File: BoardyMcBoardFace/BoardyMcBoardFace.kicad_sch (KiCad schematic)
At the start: 83 parts, among them J1 SMA, J2 ARM 10pin, J3 USB_B_Micro, SW1 SW_Push, U1 nRF24L01P, U2 STM32F103CBT6, U3 USBLC6-2SC6, U4 LM393, U5 AMS1117-5.0, U6 AMS1117-3.3, U7 USBLC6-2SC6, U8 USBLC6-2SC6, U9 TJA1051T-3, Y1 16MHz, Y2 16MHz

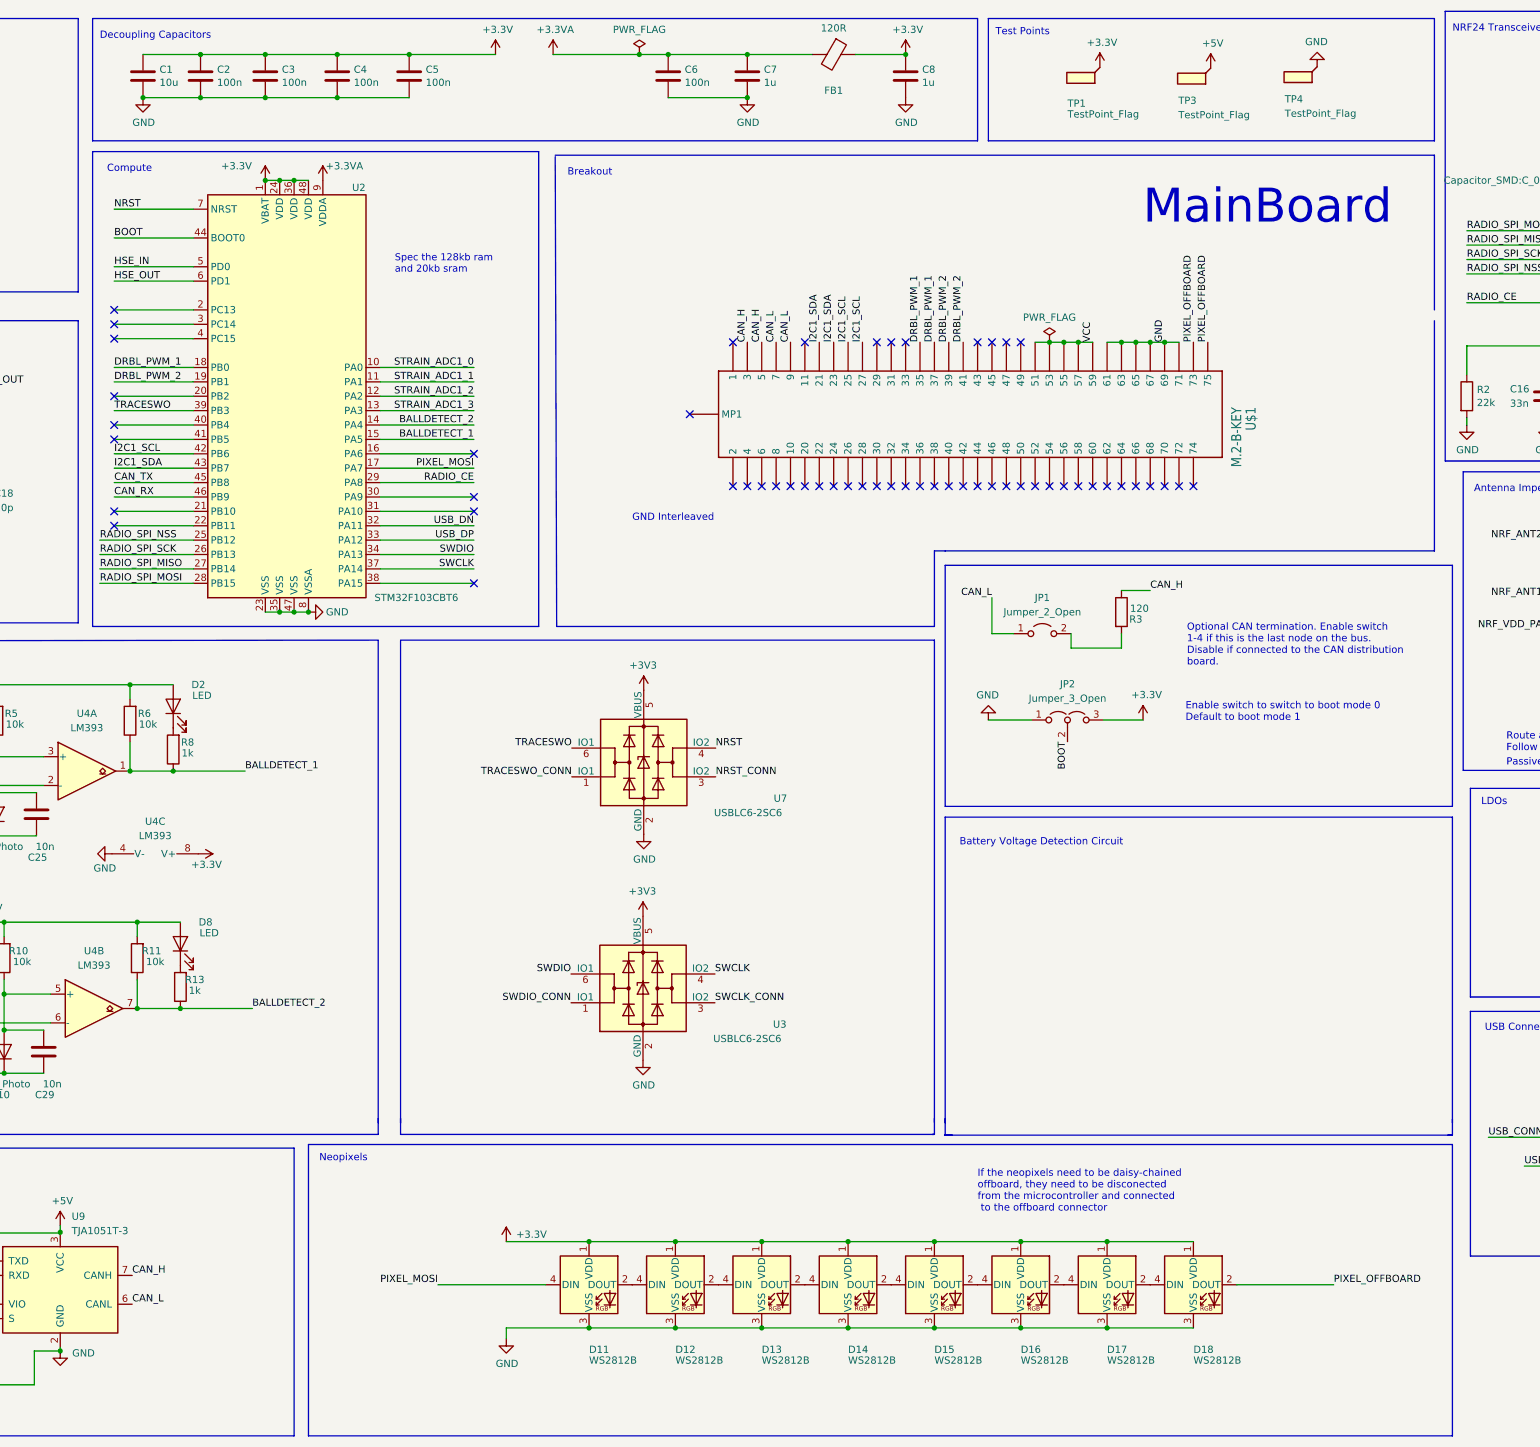
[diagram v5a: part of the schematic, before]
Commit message: changing to 2020 from 5050 neopixel changed everything
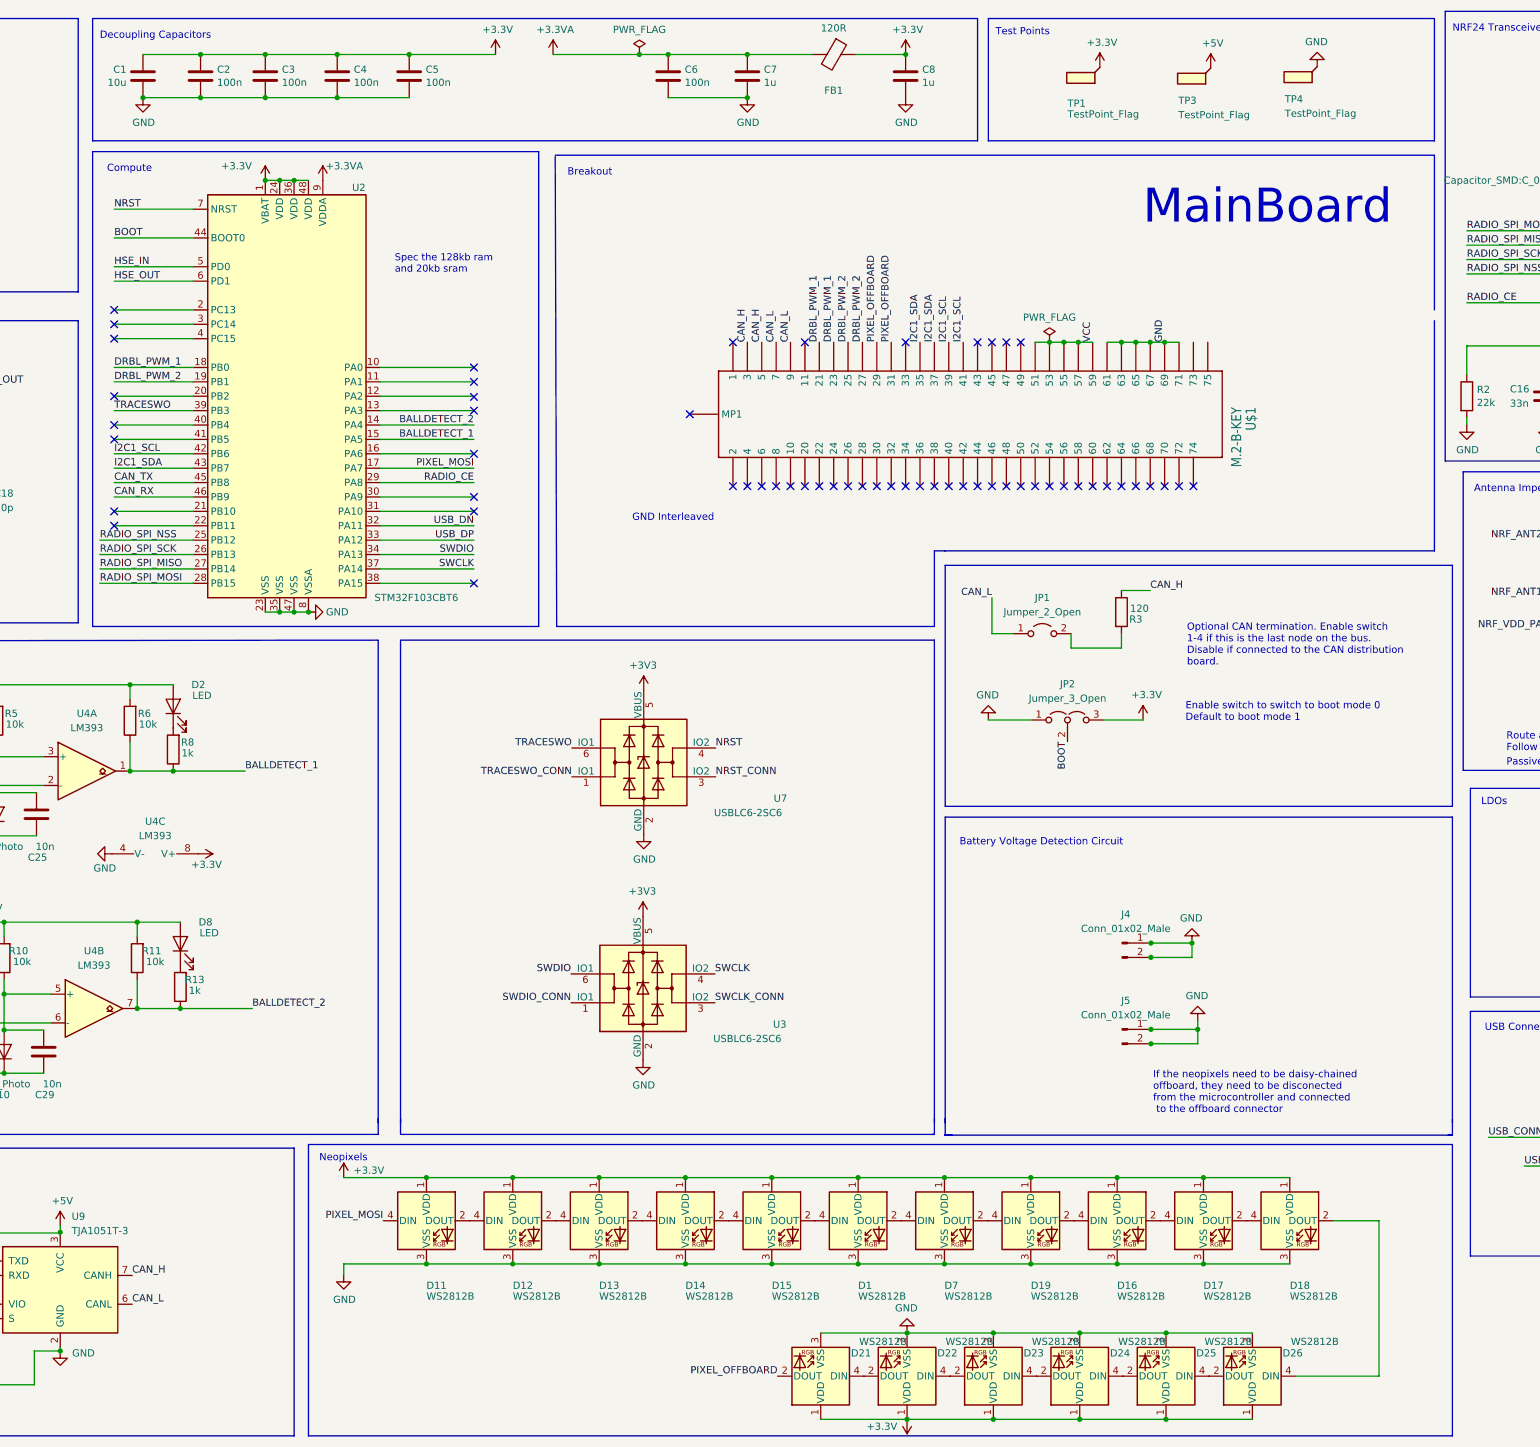
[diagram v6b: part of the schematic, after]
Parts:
- added D1, D19, D21, D22, D23, D24, D25, D26, D7: WS2812B, LED_SMD:LED_WS2812B-2020_PLCC4_2.0x2.0mm, symbol LED:WS2812B
- added J4, J5: Conn_01x02_Male, Connector_PinHeader_1.27mm:PinHeader_1x02_P1.27mm_Vertical, symbol Connector:Conn_01x02_Male
- D11, D12, D13, D14, D15, D16, D17, D18: footprint LED_SMD:LED_WS2812B_PLCC4_5.0x5.0mm_P3.2mm -> LED_SMD:LED_WS2812B-2020_PLCC4_2.0x2.0mm
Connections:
- net +3V3: now also D1.1 (VDD), D19.1 (VDD), D21.1 (VDD), D22.1 (VDD), D23.1 (VDD), D24.1 (VDD), D25.1 (VDD), D26.1 (VDD), D7.1 (VDD)
- net DRBL_PWM_1: now also U$1.P$21 (21), U$1.P$23 (23); no longer U$1.P$35 (35), U$1.P$37 (37)
- net DRBL_PWM_2: now also U$1.P$25 (25), U$1.P$27 (27); no longer U$1.P$39 (39), U$1.P$41 (41)
- net GND: now also D1.3 (VSS), D19.3 (VSS), D21.3 (VSS), D22.3 (VSS), D23.3 (VSS), D24.3 (VSS), D25.3 (VSS), D26.3 (VSS), D7.3 (VSS), J4.1 (Pin_1), J4.2 (Pin_2), J5.1 (Pin_1), J5.2 (Pin_2)
- net I2C1_SCL: now also U$1.P$39 (39), U$1.P$41 (41); no longer U$1.P$25 (25), U$1.P$27 (27)
- net I2C1_SDA: now also U$1.P$35 (35), U$1.P$37 (37); no longer U$1.P$21 (21), U$1.P$23 (23)
- net PIXEL_OFFBOARD: now also U$1.P$29 (29), U$1.P$31 (31), D21.2 (DOUT); no longer D18.2 (DOUT), U$1.P$73 (73), U$1.P$75 (75)
- net at D15.2 (DOUT): now also D1.4 (DIN); no longer D16.4 (DIN)
- net STRAIN_ADC1_0: no longer names the net of U2.10 (PA0)
- net STRAIN_ADC1_1: no longer names the net of U2.11 (PA1)
- net STRAIN_ADC1_2: no longer names the net of U2.12 (PA2)
- net STRAIN_ADC1_3: no longer names the net of U2.13 (PA3)
- new net: D16.4 (DIN), D19.2 (DOUT)
- new net: D18.2 (DOUT), D26.4 (DIN)
- new net: D19.4 (DIN), D7.2 (DOUT)
- new net: D1.2 (DOUT), D7.4 (DIN)
- new net: D24.4 (DIN), D25.2 (DOUT)
- new net: D25.4 (DIN), D26.2 (DOUT)
- new net: D23.4 (DIN), D24.2 (DOUT)
- new net: D21.4 (DIN), D22.2 (DOUT)
- new net: D22.4 (DIN), D23.2 (DOUT)
- no-connect marks 59 -> 61
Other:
- moved on the sheet: D11, D12, D13, D14, D15, D16, D17, D18

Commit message: finishing touches again??
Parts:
- added C28, C31, C32, C33, C34, C35, C36, C37, C38, C39, C40, C41, C42, C43, C44, C45, C46: 100n, Capacitor_SMD:C_0402_1005Metric, symbol Device:C
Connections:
- net +3V3: now also C28.1, C31.1, C32.1, C33.1, C34.1, C35.1, C36.1, C37.1, C38.1, C39.1, C40.1, C41.1, C42.1, C43.1, C44.1, C45.1, C46.1
- net GND: now also C28.2, C31.2, C32.2, C33.2, C34.2, C35.2, C36.2, C37.2, C38.2, C39.2, C40.2, C41.2, C42.2, C43.2, C44.2, C45.2, C46.2
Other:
- moved on the sheet: J4, J5, U3, U7

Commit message: actually final touches, ground plane ontop looks weird
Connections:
- no-connect marks 61 -> 63
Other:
- note added: "Akhil V"
- note added: "GND Probes"
- note added: "Logic analyzer and oscilliscope ground connections"
- note added: "M.2 Connector"
- note removed: "Battery Voltage Detection Circuit"
- note removed: "Breakout"
- note removed: "GND Interleaved"
- note removed: "If the neopixels need to be daisy-chained offboard, they need to be disconected from the microcontroller and connected to the offboard connector"
- note removed: "Mr.Clean"
- moved on the sheet: C20, C28, C31, C32, C33, C34, C35, C36, C37, C38, C39, C40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
